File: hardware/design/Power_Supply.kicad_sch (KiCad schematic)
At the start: 34 parts, among them J201 Screw_Terminal_01x02, SW201 SW_SPST, U201 L7805, U202 L7806, U203 L7812, U204 L7912

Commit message: Editorial change
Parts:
- renumbered C205 to C201, C206 to C202, C210 to C203, C201 to C204, C203 to C205, C207 to C206, C209 to C207, C202 to C208, C204 to C209, C208 to C210, R203 to R202, R205 to R203, R202 to R204, R204 to R205, TP203 to TP202, TP205 to TP203, TP207 to TP204, TP208 to TP205, TP202 to TP206, TP204 to TP207, TP206 to TP208

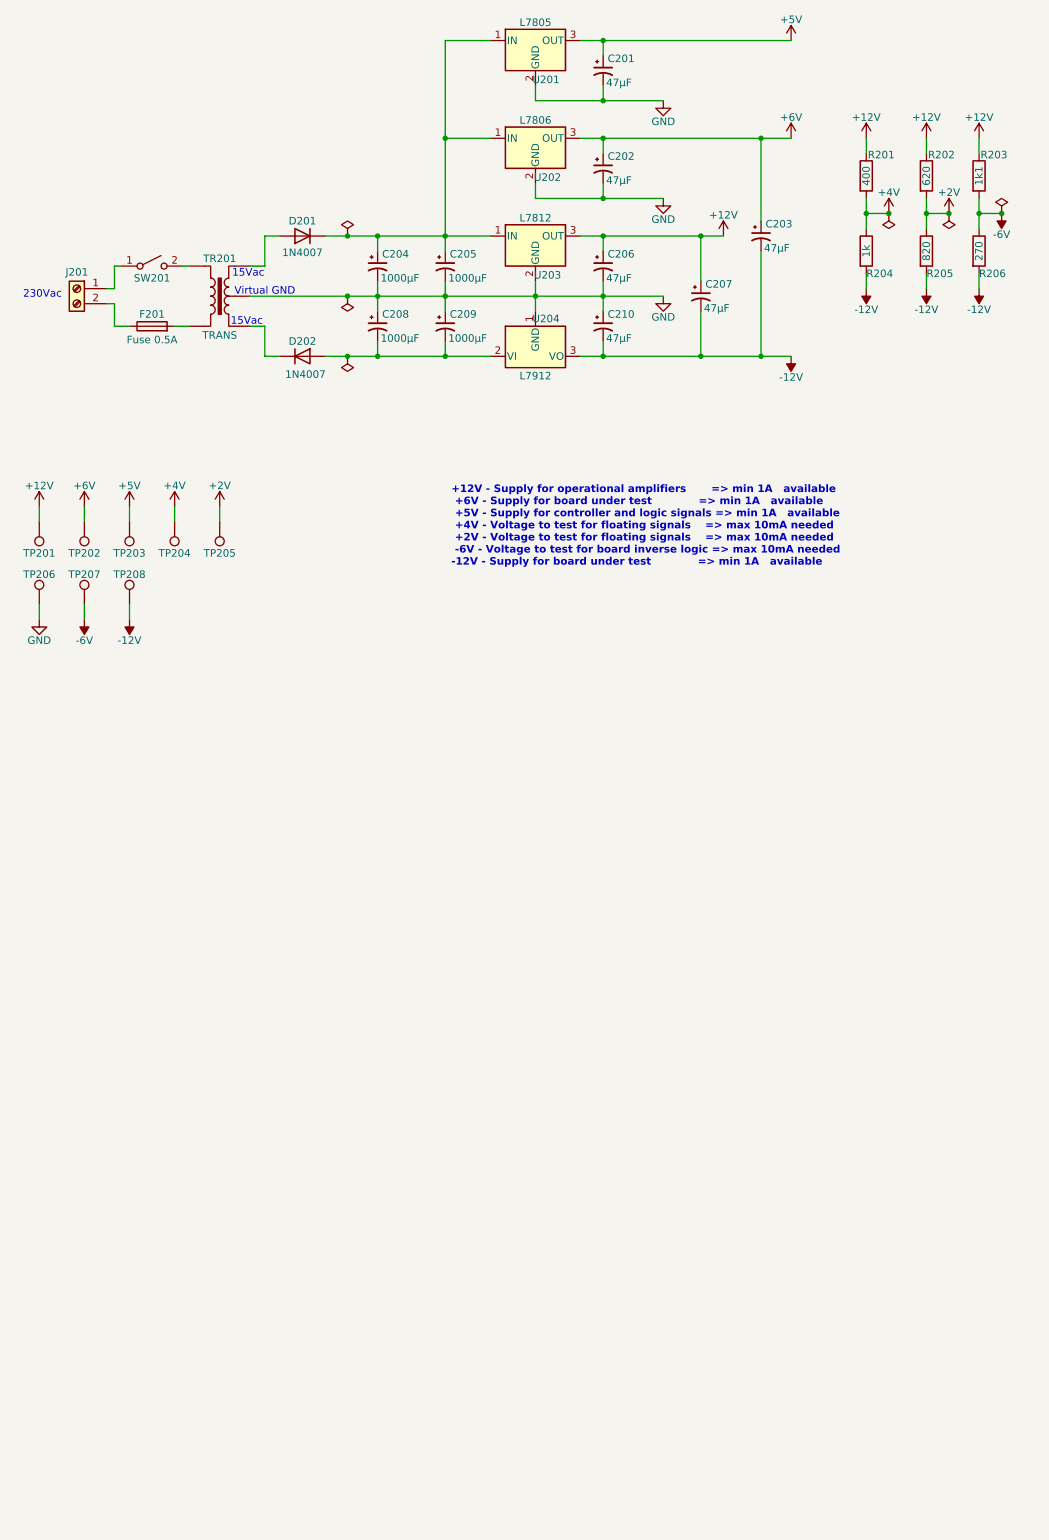
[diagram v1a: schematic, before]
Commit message: Replaced solid state relay with electromechanical relay
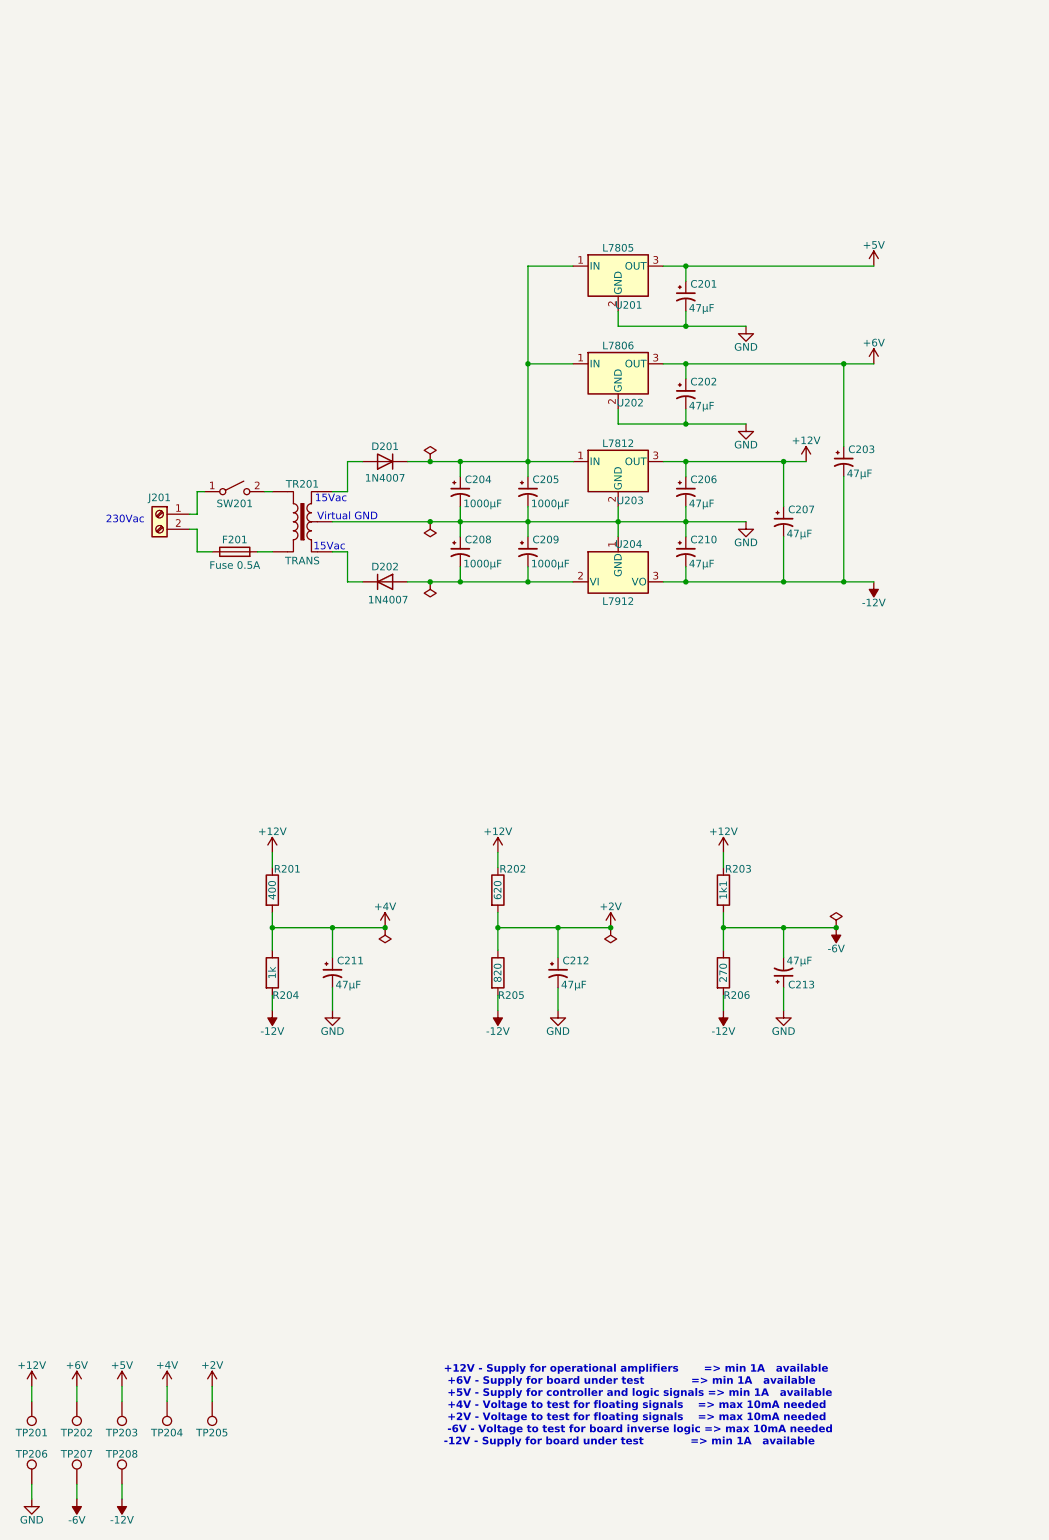
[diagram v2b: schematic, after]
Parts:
- added C211, C212, C213: 47µF, Capacitor_THT:CP_Radial_D8.0mm_P5.00mm, symbol Device:C_Polarized_Small_US
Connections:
- net +2V: now also C212.1
- net +4V: now also C211.1
- net -6V: now also C213.2
- net GND: now also C211.2, C212.2, C213.1
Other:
- moved on the sheet: C201, C202, C203, C204, C205, C206, C207, C208, C209, C210, D201, D202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

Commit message: Simulating alternative power supply
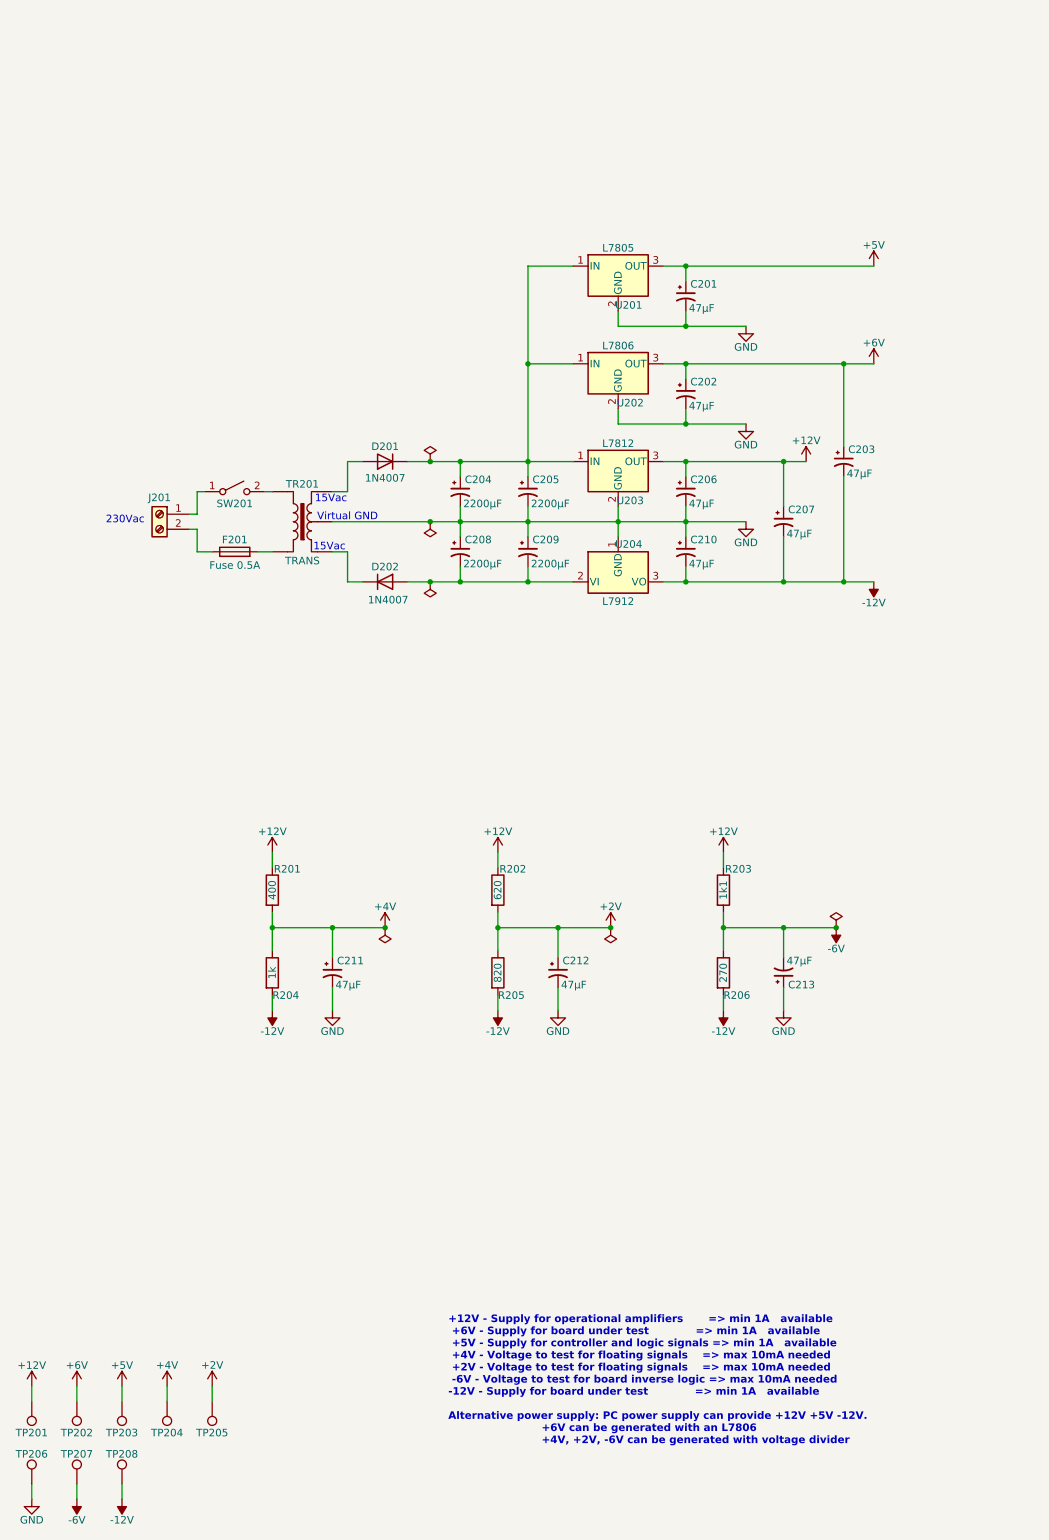
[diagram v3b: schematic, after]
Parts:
- C204, C205, C208, C209: value 1000µF -> 2200µF
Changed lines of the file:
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@@
 		)
 	)
-	(text "+12V - Supply for operational amplifiers       => min 1A   available\n +6V - Supply for board under test             => min 1A   available\n +5V - Supply for controller and logic signals => min 1A   available\n +4V - Voltage to test for floating signals    => max 10mA needed\n +2V - Voltage to test for floating signals    => max 10mA needed\n -6V - Voltage to test for board inverse logic => max 10mA needed\n-12V - Supply for board under test             => min 1A   available"
+	(text "+12V - Supply for operational amplifiers       => min 1A   available\n +6V - Supply for board under test             => min 1A   available\n +5V - Supply for controller and logic signals => min 1A   available\n +4V - Voltage to test for floating signals    => max 10mA needed\n +2V - Voltage to test for floating signals    => max 10mA needed\n -6V - Voltage to test for board inverse logic => max 10mA needed\n-12V - Supply for board under test             => min 1A   available\n\nAlternative power supply: PC power supply can provide +12V +5V -12V.\n                          +6V can be generated with an L7806\n                          +4V, +2V, -6V can be generated with voltage divider"
 		(exclude_from_sim no)
-		(at 89.916 252.984 0)
+		(at 90.678 244.602 0)
 		(effects
 			(font
@@
 			)
 		)
-		(property "Value" "1000µF"
+		(property "Value" "2200µF"
 			(at 93.218 117.602 0)
 			(effects
@@
 			)
 		)
-		(property "Value" "1000µF"
+		(property "Value" "2200µF"
 			(at 104.648 107.442 0)
 			(effects
@@
 			)
 		)
-		(property "Value" "1000µF"
+		(property "Value" "2200µF"
 			(at 93.218 107.442 0)
 			(effects
@@
 			)
 		)
-		(property "Value" "1000µF"
+		(property "Value" "2200µF"
 			(at 104.648 117.602 0)
 			(effects

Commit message: File cleanup
Added final schematics
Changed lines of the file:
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@@
 	(title_block
 		(title "VersaLogic board tester")
-		(date "2025-08-13")
-		(rev "1.0.alpha")
+		(date "2025-09-09")
+		(rev "1.0")
 		(comment 1 "Copyright (c) 2025 by Filip Pynckels & Robin Pynckels")
 	)
@@
 		)
 	)
-	(text "+12V - Supply for operational amplifiers       => min 1A   available\n +6V - Supply for board under test             => min 1A   available\n +5V - Supply for controller and logic signals => min 1A   available\n +4V - Voltage to test for floating signals    => max 10mA needed\n +2V - Voltage to test for floating signals    => max 10mA needed\n -6V - Voltage to test for board inverse logic => max 10mA needed\n-12V - Supply for board under test             => min 1A   available\n\nAlternative power supply: PC power supply can provide +12V +5V -12V.\n                          +6V can be generated with an L7806\n                          +4V, +2V, -6V can be generated with voltage divider"
+	(text "+12V - Supply for operational amplifiers       => min 1A   available\n +6V - Supply for board under test             => min 1A   available\n +5V - Supply for controller and logic signals => min 1A   available\n +4V - Voltage to test for floating signals    => max 10mA needed\n +2V - Voltage to test for floating signals    => max 10mA needed\n -6V - Voltage to test for board inverse logic => max 10mA needed\n-12V - Supply for board under test             => min 1A   available\n\nAlternative power supply: PC power supply can provide +12V +5V -12V.\n                          +6V can be generated with an L7806\n                          +4V, +2V, -6V can be generated with voltage divider\n\nNote: The pins +12V, +6V, +5V, +4V, +2V, GND, -6V, -12V are global pins. When\n      dividing the PCB in multiple parts the necessary power supply pins have\n      to be passed to the different boards into which the PCB is divided.\n      One method to do this is to create a \"power bus\" that passes all power\n      supply rails to the different PCB's."
 		(exclude_from_sim no)
-		(at 90.678 244.602 0)
+		(at 90.424 231.902 0)
 		(effects
 			(font
